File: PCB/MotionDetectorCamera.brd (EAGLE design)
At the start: 41.9 x 32.6 mm, 185 parts, among them J1 JUMPER-SOLDER, J10 MICROSD-SOCKET, J11 USB-C-JACK, J2 JUMPER-SOLDER, J3 JUMPER-SOLDER, J4 JUMPER-SOLDER, J5 JST-SM02B-SRSS-TB, J6 JUMPER-SOLDER, J7 JUMPER-SOLDER, J8 JUMPER-SOLDER, J9 S-MOUNT-LENS-HOLDERM12LENSES-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, Q1 PMOS-NEXPERIA-SOT1220, Q2 PMOS-NEXPERIA-SOT1220, Q3 PMOS-NEXPERIA-SOT1220, U1 TI-TPS2116, U10 TI-TPS22919DCK, U11 TI-TPS62A01, U13 TI-TPS22919DCK, U14 TI-TPS22919DCK, U15 TI-MSP430FR2422IRHL, U16 NXP-NTB0102, U17 NXP-NTB0102, U18 PANASONIC-EKMB110711X, U19 LATTICE-ICE40HX4K-BG121, U2 DIODESINC-AP7350, U20 WINBOND-W25Q40EW, U21 NEXPERIA-74LVC1G98-OR-INV-INP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, U22 NEXPERIA-74LVC1G98-BUFFER, U23 ON-AR0330CS1C12SPKA0, U24 ALLIANCE-AS4C8M16MSA-6BIN, U25 STM-STM32F730, U26 DIODESINC-DT1446-04V-7, U27 NEXPERIA-74LVC1G98-BUFFER, U3 NEXPERIA-74LVC1G98-NOR, U4 MICROCHIP-MCP7383X, U5 EATON-STN101, U6 TI-TPS62A01, U7 TI-TPS62A01, U9 TI-TPS22919DCK, X1 EPSON-FC-135, X2 SITIME-SIT8021, X3 SITIME-SIT8021

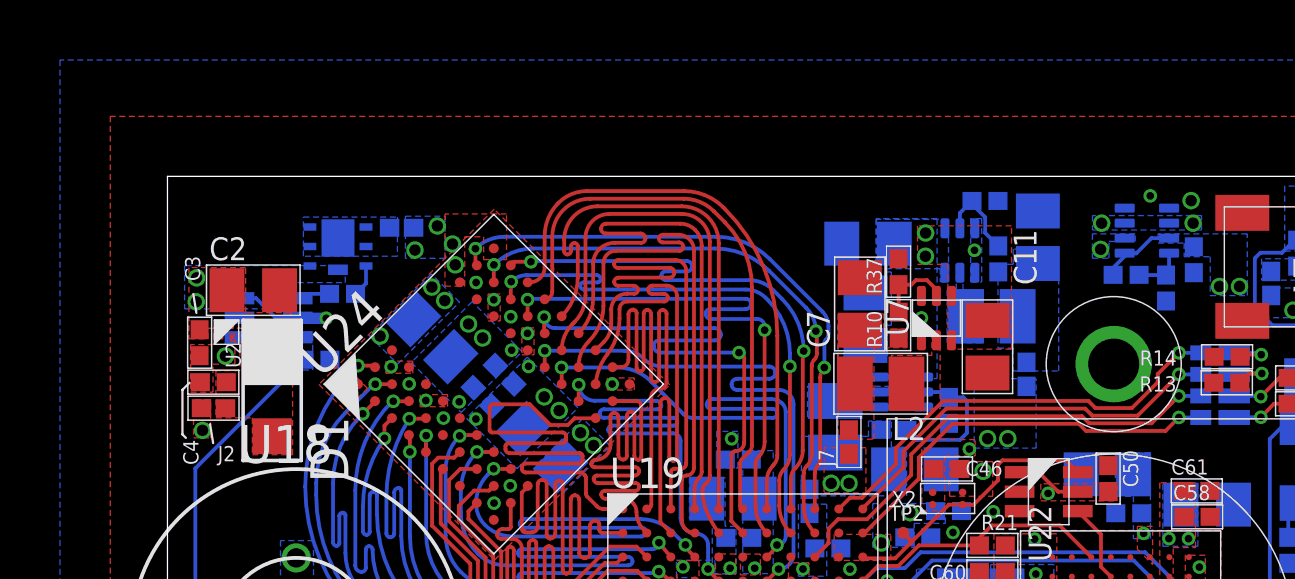
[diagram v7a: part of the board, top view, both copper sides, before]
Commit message: 12 airwires
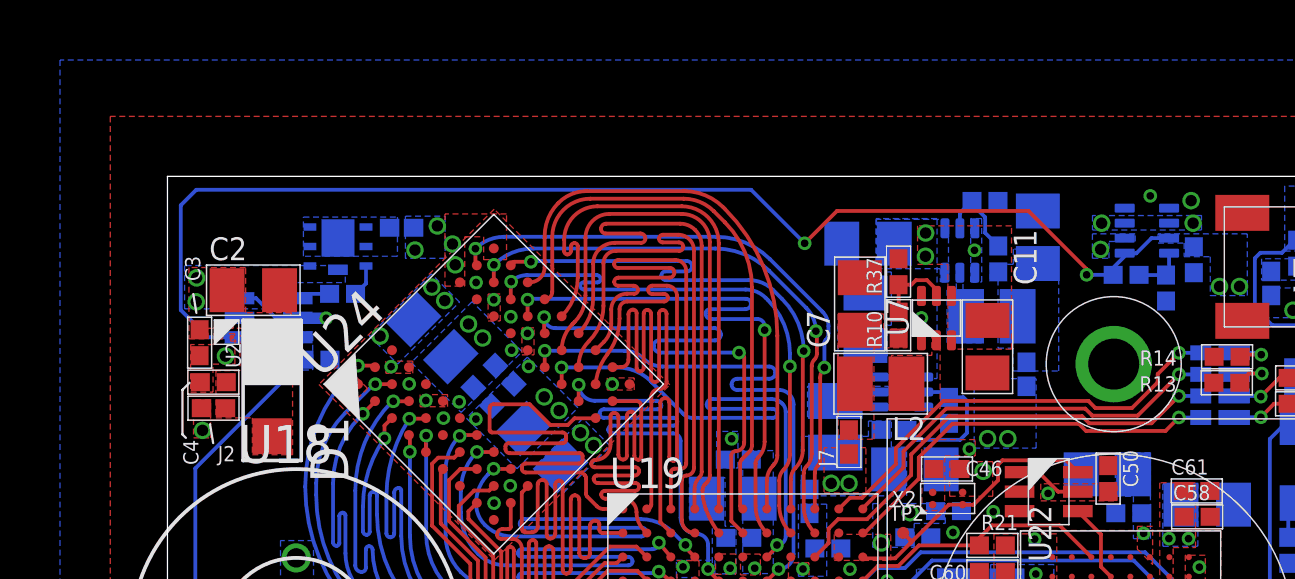
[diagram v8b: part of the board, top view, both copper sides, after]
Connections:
- net STM_LED0: no longer U25.P14
- net STM_LED1: no longer U25.N14
- net STM_LED2: no longer U25.M14
- net STM_LED3: no longer U25.L14
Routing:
- net VDD_USB: track 38.9 -> 78.3 mm, vias 8 -> 10
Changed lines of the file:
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@@
 <signal name="STM_LED0">
 <contactref element="LED8" pad="A"/>
-<contactref element="U25" pad="P14"/>
 <contactref element="U25" pad="R12"/>
 <wire x1="25.530403125" y1="9.87901875" x2="25.530403125" y2="10.115903125" width="0.127" layer="16"/>
@@
 <wire x1="37.00018125" y1="13.9805875" x2="37.451696875" y2="14.432103125" width="0.127" layer="16"/>
 <wire x1="37.451696875" y1="14.432103125" x2="38.089171875" y2="14.432103125" width="0.127" layer="16"/>
-<wire x1="25.530403125" y1="9.87901875" x2="26.830403125" y2="9.22901875" width="0" layer="19" extent="16-16"/>
 </signal>
 <signal name="N$54">
@@
 <wire x1="39.63161875" y1="18.52421875" x2="39.9923" y2="18.8849" width="0.635" layer="15"/>
 <wire x1="39.63161875" y1="18.52421875" x2="39.309040625" y2="18.52421875" width="0.635" layer="15"/>
-<wire x1="25.654" y1="10.922" x2="2.4022375" y2="27.286703125" width="0" layer="19" extent="16-16"/>
+<wire x1="2.4022375" y1="27.286703125" x2="1.351796875" y2="27.286703125" width="0.127" layer="16"/>
+<wire x1="1.351796875" y1="27.286703125" x2="0.4445" y2="28.194" width="0.127" layer="16"/>
+<wire x1="0.4445" y1="28.194" x2="0.4445" y2="31.6865" width="0.127" layer="16"/>
+<wire x1="0.4445" y1="31.6865" x2="0.96011875" y2="32.20211875" width="0.127" layer="16"/>
+<wire x1="31.5231" y1="29.36688125" x2="30.83111875" y2="29.36688125" width="0.127" layer="16"/>
+<wire x1="30.83111875" y1="29.36688125" x2="30.734" y2="29.464" width="0.127" layer="16"/>
+<wire x1="30.734" y1="29.464" x2="30.63904375" y2="29.36904375" width="0.127" layer="16"/>
+<via x="30.63904375" y="29.36904375" extent="1-16" drill="0.254"/>
+<wire x1="19.4564" y1="32.20211875" x2="21.239478125" y2="30.419040625" width="0.127" layer="16"/>
+<via x="21.239478125" y="30.419040625" extent="1-16" drill="0.254"/>
+<wire x1="0.96011875" y1="32.20211875" x2="19.4564" y2="32.20211875" width="0.127" layer="16"/>
+<wire x1="21.239478125" y1="30.419040625" x2="22.3164375" y2="31.496" width="0.127" layer="1"/>
+<wire x1="22.3164375" y1="31.496" x2="28.702" y2="31.496" width="0.127" layer="1"/>
+<wire x1="28.702" y1="31.496" x2="30.63904375" y2="29.55895625" width="0.127" layer="1"/>
+<wire x1="30.63904375" y1="29.55895625" x2="30.63904375" y2="29.36904375" width="0.127" layer="1"/>
 </signal>
 <signal name="VDD_B_1V8_STM">
@@
 <signal name="STM_LED1">
 <contactref element="LED7" pad="A"/>
-<contactref element="U25" pad="N14"/>
 <contactref element="U25" pad="P12"/>
 <wire x1="26.3906" y1="10.6168875" x2="26.3906" y2="11.2993875" width="0.127" layer="16"/>
@@
 <wire x1="37.491975" y1="13.692175" x2="38.089171875" y2="13.692175" width="0.127" layer="16"/>
 <wire x1="26.67213125" y1="11.58091875" x2="36.23630625" y2="11.58091875" width="0.127" layer="16"/>
-<wire x1="25.530403125" y1="9.22901875" x2="26.830403125" y2="8.57901875" width="0" layer="19" extent="16-16"/>
 </signal>
 <signal name="STM_LED2">
 <contactref element="LED6" pad="A"/>
-<contactref element="U25" pad="M14"/>
 <contactref element="U25" pad="R13"/>
 <wire x1="26.180403125" y1="9.87901875" x2="26.180403125" y2="10.047478125" width="0.127" layer="16"/>
@@
 <wire x1="37.51071875" y1="12.74456875" x2="37.718396875" y2="12.952246875" width="0.127" layer="16"/>
 <wire x1="37.718396875" y1="12.952246875" x2="38.089171875" y2="12.952246875" width="0.127" layer="16"/>
-<wire x1="26.180403125" y1="9.87901875" x2="26.830403125" y2="7.92901875" width="0" layer="19" extent="16-16"/>
 </signal>
 <signal name="STM_LED3">
 <contactref element="LED5" pad="A"/>
-<contactref element="U25" pad="L14"/>
 <contactref element="U25" pad="P13"/>
 <wire x1="26.4709" y1="9.7586875" x2="26.4709" y2="9.9787625" width="0.127" layer="16"/>
@@
 <wire x1="36.949771875" y1="11.07291875" x2="38.089171875" y2="12.21231875" width="0.127" layer="16"/>
 <wire x1="27.13655625" y1="11.07291875" x2="36.949771875" y2="11.07291875" width="0.127" layer="16"/>
-<wire x1="26.830403125" y1="7.27901875" x2="26.180403125" y2="9.22901875" width="0" layer="19" extent="16-16"/>
 </signal>
 <signal name="MSP_TEST_X">
@@
 <wire x1="27.256496875" y1="31.287715625" x2="26.8191625" y2="31.72505" width="0.127" layer="16"/>
 <wire x1="26.8191625" y1="31.831278125" x2="26.416" y2="31.428115625" width="0.127" layer="16"/>
-<wire x1="26.416" y1="31.428115625" x2="26.416" y2="30.917740625" width="0.127" layer="16"/>
+<wire x1="26.416" y1="30.917740625" x2="26.416" y2="31.428115625" width="0.127" layer="16"/>
 </signal>
 <signal name="N$13">
